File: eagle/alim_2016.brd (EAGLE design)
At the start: 66.5 x 50 mm, 72 parts, among them J1 AVR_SPI_PRG_6PTH, U1 ATMEGA328P_TQFP, U2 TPS54821RHLR, U3 IRFR8314TRPBF, U4 IRFR8314TRPBF, U5 3.3V

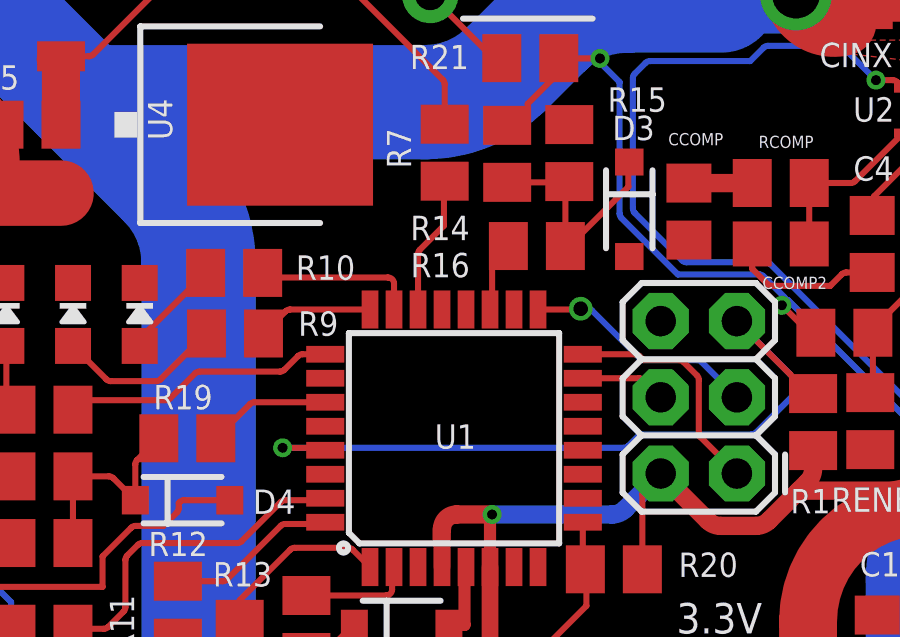
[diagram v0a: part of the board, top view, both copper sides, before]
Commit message: fix routing error: ADC7 cannot be a GPIO
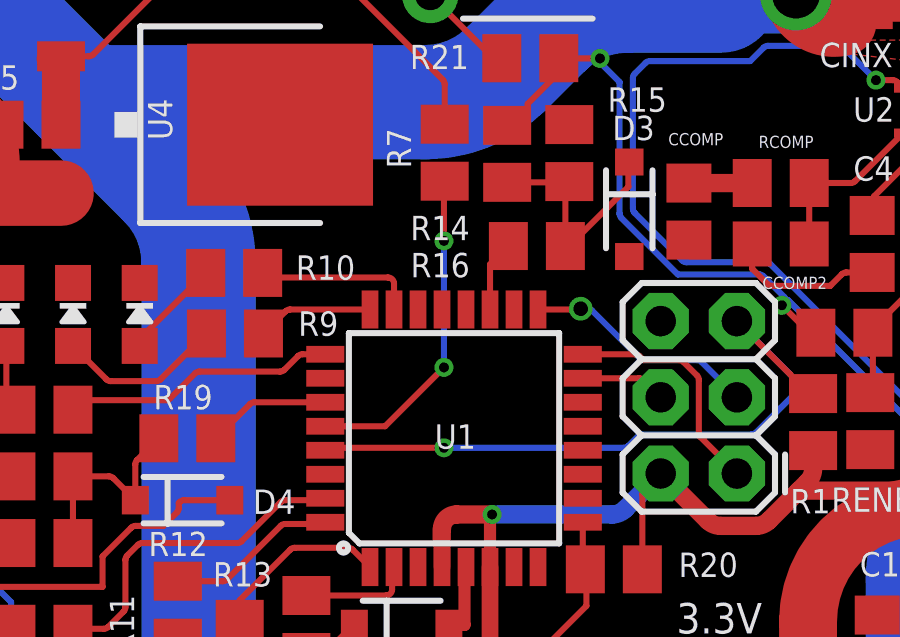
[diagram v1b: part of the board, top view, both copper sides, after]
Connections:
- net N$2 renamed SCK
- net N$3 renamed MISO
- net N$4 renamed MOSI
- net N$23: now also U1.28; no longer U1.22
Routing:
- net N$23: track 4.63 -> 11.0 mm, vias 0 -> 2
- net RESET: track 26.2 -> 23.5 mm
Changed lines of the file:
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@@
 <?xml version="1.0" encoding="utf-8"?>
 <!DOCTYPE eagle SYSTEM "eagle.dtd">
-<eagle version="7.3.0">
+<eagle version="7.5.0">
 <drawing>
 <settings>
@@
 <setting verticaltext="up"/>
 </settings>
-<grid distance="0.001" unitdist="inch" unit="inch" style="lines" multiple="1" display="no" altdistance="25" altunitdist="mil" altunit="mil"/>
+<grid distance="2" unitdist="mil" unit="mil" style="lines" multiple="1" display="no" altdistance="25" altunitdist="mil" altunit="mil"/>
 <layers>
 <layer number="1" name="Top" color="4" fill="1" visible="yes" active="yes"/>
@@
 <layer number="20" name="Dimension" color="15" fill="1" visible="yes" active="yes"/>
 <layer number="21" name="tPlace" color="7" fill="1" visible="yes" active="yes"/>
-<layer number="22" name="bPlace" color="7" fill="1" visible="yes" active="yes"/>
+<layer number="22" name="bPlace" color="7" fill="1" visible="no" active="yes"/>
 <layer number="23" name="tOrigins" color="15" fill="1" visible="yes" active="yes"/>
 <layer number="24" name="bOrigins" color="15" fill="1" visible="yes" active="yes"/>
 <layer number="25" name="tNames" color="7" fill="1" visible="yes" active="yes"/>
-<layer number="26" name="bNames" color="7" fill="1" visible="yes" active="yes"/>
+<layer number="26" name="bNames" color="7" fill="1" visible="no" active="yes"/>
 <layer number="27" name="tValues" color="7" fill="1" visible="yes" active="yes"/>
-<layer number="28" name="bValues" color="7" fill="1" visible="yes" active="yes"/>
-<layer number="29" name="tStop" color="7" fill="3" visible="yes" active="yes"/>
-<layer number="30" name="bStop" color="7" fill="6" visible="yes" active="yes"/>
-<layer number="31" name="tCream" color="7" fill="4" visible="yes" active="yes"/>
-<layer number="32" name="bCream" color="7" fill="5" visible="yes" active="yes"/>
-<layer number="33" name="tFinish" color="6" fill="3" visible="yes" active="yes"/>
-<layer number="34" name="bFinish" color="6" fill="6" visible="yes" active="yes"/>
-<layer number="35" name="tGlue" color="7" fill="4" visible="yes" active="yes"/>
-<layer number="36" name="bGlue" color="7" fill="5" visible="yes" active="yes"/>
-<layer number="37" name="tTest" color="7" fill="1" visible="yes" active="yes"/>
-<layer number="38" name="bTest" color="7" fill="1" visible="yes" active="yes"/>
-<layer number="39" name="tKeepout" color="4" fill="11" visible="yes" active="yes"/>
-<layer number="40" name="bKeepout" color="1" fill="11" visible="yes" active="yes"/>
-<layer number="41" name="tRestrict" color="4" fill="10" visible="yes" active="yes"/>
-<layer number="42" name="bRestrict" color="1" fill="10" visible="yes" active="yes"/>
-<layer number="43" name="vRestrict" color="2" fill="10" visible="yes" active="yes"/>
+<layer number="28" name="bValues" color="7" fill="1" visible="no" active="yes"/>
+<layer number="29" name="tStop" color="7" fill="3" visible="no" active="yes"/>
+<layer number="30" name="bStop" color="7" fill="6" visible="no" active="yes"/>
+<layer number="31" name="tCream" color="7" fill="4" visible="no" active="yes"/>
+<layer number="32" name="bCream" color="7" fill="5" visible="no" active="yes"/>
+<layer number="33" name="tFinish" color="6" fill="3" visible="no" active="yes"/>
+<layer number="34" name="bFinish" color="6" fill="6" visible="no" active="yes"/>
+<layer number="35" name="tGlue" color="7" fill="4" visible="no" active="yes"/>
+<layer number="36" name="bGlue" color="7" fill="5" visible="no" active="yes"/>
+<layer number="37" name="tTest" color="7" fill="1" visible="no" active="yes"/>
+<layer number="38" name="bTest" color="7" fill="1" visible="no" active="yes"/>
+<layer number="39" name="tKeepout" color="4" fill="11" visible="no" active="yes"/>
+<layer number="40" name="bKeepout" color="1" fill="11" visible="no" active="yes"/>
+<layer number="41" name="tRestrict" color="4" fill="10" visible="no" active="yes"/>
+<layer number="42" name="bRestrict" color="1" fill="10" visible="no" active="yes"/>
+<layer number="43" name="vRestrict" color="2" fill="10" visible="no" active="yes"/>
 <layer number="44" name="Drills" color="7" fill="1" visible="yes" active="yes"/>
 <layer number="45" name="Holes" color="7" fill="1" visible="yes" active="yes"/>
@@
 </class>
 </classes>
-<designrules name="ShenZhen2U EagleRules">
+<designrules name="ShenZhen2U EagleRules *">
 <description language="de">
 &lt;b&gt;EAGLE Design Rules&lt;/b&gt;
@@
 <param name="dpGapFactor" value="2.5"/>
 <param name="checkGrid" value="0"/>
-<param name="checkAngle" value="0"/>
+<param name="checkAngle" value="1"/>
 <param name="checkFont" value="1"/>
 <param name="checkRestrict" value="0"/>
@@
 <wire x1="43.9609" y1="13.244" x2="43.8303" y2="13.8754" width="0.2032" layer="1" curve="90"/>
 </signal>
-<signal name="N$2">
+<signal name="SCK">
 <contactref element="J1" pad="3"/>
 <contactref element="U1" pad="17"/>
@@
 <wire x1="38.000765625" y1="31.118984375" x2="39.1795" y2="29.94025" width="0.2032" layer="16"/>
 </signal>
-<signal name="N$3">
+<signal name="MISO">
 <contactref element="J1" pad="1"/>
 <contactref element="U1" pad="16"/>
@@
 <wire x1="37.969015625" y1="28.610734375" x2="39.1795" y2="27.40025" width="0.2032" layer="1"/>
 </signal>
-<signal name="N$4">
+<signal name="MOSI">
 <contactref element="J1" pad="4"/>
 <contactref element="U1" pad="15"/>
@@
 <contactref element="U1" pad="29"/>
 <wire x1="25.45715" y1="28.175" x2="25.37465" y2="28.2575" width="0.2032" layer="1"/>
-<wire x1="25.37465" y1="28.2575" x2="24.03475" y2="28.2575" width="0.2032" layer="1"/>
-<via x="24.03475" y="28.2575" extent="1-16" drill="0.3302"/>
+<wire x1="25.37465" y1="28.2575" x2="29.4132" y2="28.2575" width="0.2032" layer="1"/>
+<via x="29.4132" y="28.2575" extent="1-16" drill="0.3302"/>
 <wire x1="41.021" y1="30.55458125" x2="40.961484375" y2="30.698265625" width="0.2032" layer="1" curve="45"/>
 <wire x1="40.961484375" y1="30.698265625" x2="39.1795" y2="32.48025" width="0.2032" layer="1"/>
-<wire x1="24.03475" y1="28.2575" x2="35.41233125" y2="28.2575" width="0.2032" layer="16"/>
+<wire x1="29.4132" y1="28.2575" x2="35.41233125" y2="28.2575" width="0.2032" layer="16"/>
 <wire x1="35.41233125" y1="28.2575" x2="35.556015625" y2="28.317015625" width="0.2032" layer="16" curve="45"/>
 <wire x1="35.556015625" y1="28.317015625" x2="35.941" y2="28.702" width="0.2032" layer="16"/>
@@
 <wire x1="33.6630375" y1="35.1831875" x2="33.462" y2="34.98215" width="0.2032" layer="1"/>
 </signal>
-<signal name="N$27">
-<contactref element="U1" pad="19"/>
-<contactref element="R16" pad="2"/>
-<wire x1="30.94975" y1="32.8676" x2="31.01975" y2="32.9376" width="0.2032" layer="1"/>
-<wire x1="31.01975" y1="32.9376" x2="31.01975" y2="34.58433125" width="0.2032" layer="1"/>
-<wire x1="31.01975" y1="34.58433125" x2="31.079265625" y2="34.728015625" width="0.2032" layer="1" curve="-45"/>
-<wire x1="31.562" y1="34.98215" x2="31.41756875" y2="34.98215" width="0.2032" layer="1"/>
-<wire x1="31.41756875" y1="34.98215" x2="31.273884375" y2="34.922634375" width="0.2032" layer="1" curve="45"/>
-<wire x1="31.273884375" y1="34.922634375" x2="31.079265625" y2="34.728015625" width="0.2032" layer="1"/>
-</signal>
 <signal name="BAT24_SENSE">
 <contactref element="R17" pad="1"/>
@@
 </signal>
 <signal name="N$23">
-<contactref element="U1" pad="22"/>
 <contactref element="R7" pad="2"/>
 <wire x1="29.4386" y1="37.14365" x2="29.4132" y2="37.082328125" width="0.2032" layer="1" curve="45"/>
-<wire x1="29.4132" y1="37.082328125" x2="29.4132" y2="35.6616" width="0.2032" layer="1"/>
-<wire x1="29.4132" y1="35.6616" x2="28.609265625" y2="34.857665625" width="0.2032" layer="1"/>
-<wire x1="28.609265625" y1="34.857665625" x2="28.54975" y2="34.71398125" width="0.2032" layer="1" curve="45"/>
-<wire x1="28.54975" y1="34.71398125" x2="28.54975" y2="32.8676" width="0.2032" layer="1"/>
+<wire x1="29.4132" y1="37.082328125" x2="29.4132" y2="35.1536" width="0.2032" layer="1"/>
+<contactref element="U1" pad="28"/>
+<wire x1="25.45715" y1="28.975" x2="27.451" y2="28.975" width="0.2032" layer="1"/>
+<wire x1="27.451" y1="28.975" x2="29.4132" y2="30.9372" width="0.2032" layer="1"/>
+<via x="29.4132" y="30.9372" extent="1-16" drill="0.3302" diameter="0.2032"/>
+<wire x1="29.4132" y1="30.9372" x2="29.4132" y2="35.1536" width="0.2032" layer="16"/>
+<via x="29.4132" y="35.1536" extent="1-16" drill="0.3302" diameter="0.2032"/>
 </signal>
 <signal name="N$28">
@@
 <wire x1="30.861" y1="16.129" x2="29.5148" y2="16.129" width="0.2032" layer="1"/>
 </signal>
+<signal name="N$2">
+<contactref element="R16" pad="2"/>
+<contactref element="U1" pad="19"/>
+<wire x1="30.94975" y1="32.8676" x2="30.94975" y2="34.3699" width="0.2032" layer="1"/>
+<wire x1="30.94975" y1="34.3699" x2="31.562" y2="34.98215" width="0.2032" layer="1"/>
+</signal>
 </signals>
